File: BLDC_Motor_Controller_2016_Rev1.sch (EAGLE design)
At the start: 99 parts, among them J1 SERVOMOLEX_SL_THRU_HOLE, J2 SL03THROUGH_HOLE, J3 APP_2POS_CONFIG5V_HORIZ, Q1 MOSFET-NCHANNELFQP30N06L, Q2 MOSFET-NCHANNELFQP30N06L, Q3 MOSFET-NCHANNELFQP30N06L, Q4 MOSFET-NCHANNELFQP30N06L, Q5 MOSFET-NCHANNELFQP30N06L, Q6 MOSFET-NCHANNELFQP30N06L, Q7 MOSFET-PCHANNEL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

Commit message: Added RS-485 IC to replace UART
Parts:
- removed J2: SL03THROUGH_HOLE, MRDT-Connectors:SL03THROUGH_HOLE
- added R30, R31: 3.3, SparkFun-Passives:RESISTOR0805-RES
- added U$3: MAX3077, MRDT-2015-General:MAX3077
- added U$4: 5PIN, Molex-SL:5PIN
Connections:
- new net N$34: R30.2, U$3.Y, U$4.4
- new net N$36: R30.1, U$3.Z, U$4.3
- new net N$37: R31.2, U$3.B, U$4.2
- new net N$38: R31.1, U$3.A, U$4.1
- net GND: now also U$3.GND, U$4.5; no longer J2.1
- net RX: now also U$3.RO; no longer J2.2
- net TX: now also U$3.DI; no longer J2.3
- net VCC: now also U$3.VCC
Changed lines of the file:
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@@
 <?xml version="1.0" encoding="utf-8"?>
 <!DOCTYPE eagle SYSTEM "eagle.dtd">
-<eagle version="7.3.0">
+<eagle version="7.1.0">
 <drawing>
 <settings>
@@
 <part name="C35" library="SparkFun-Passives" deviceset="CAP_POL" device="PTH4" value="220u"/>
 <part name="GND35" library="SparkFun-Aesthetics" deviceset="GND" device=""/>
-<part name="J2" library="MRDT-Connectors" deviceset="SL03" device="THROUGH_HOLE"/>
-<part name="GND34" library="SparkFun-Aesthetics" deviceset="GND" device=""/>
 <part name="J1" library="MRDT-Connectors" deviceset="SERVO" device="MOLEX_SL_THRU_HOLE"/>
 <part name="J3" library="MRDT-Connectors" deviceset="APP_2POS_CONFIG" device="5V_HORIZ"/>
 <part name="C38" library="SparkFun-Passives" deviceset="CAP_POL" device="PTH4" value="220u"/>
+<part name="U$3" library="MRDT-2015-General" deviceset="MAX3077" device=""/>
+<part name="R30" library="SparkFun-Passives" deviceset="RESISTOR" device="0805-RES" value="3.3"/>
+<part name="R31" library="SparkFun-Passives" deviceset="RESISTOR" device="0805-RES" value="3.3"/>
+<part name="U$4" library="Molex-SL" deviceset="5PIN" device=""/>
+<part name="GND36" library="SparkFun-Aesthetics" deviceset="GND" device=""/>
+<part name="GND37" library="SparkFun-Aesthetics" deviceset="GND" device=""/>
 </parts>
 <sheets>
@@
 <instance part="C35" gate="G$1" x="-63.5" y="-121.92"/>
 <instance part="GND35" gate="1" x="274.32" y="-195.58"/>
-<instance part="J2" gate="G$1" x="289.56" y="-167.64"/>
-<instance part="GND34" gate="1" x="276.86" y="-175.26"/>
 <instance part="J1" gate="G$1" x="284.48" y="-193.04"/>
 <instance part="J3" gate="GND" x="256.54" y="-53.34"/>
 <instance part="J3" gate="VCC" x="256.54" y="-45.72"/>
 <instance part="C38" gate="G$1" x="-73.66" y="-121.92"/>
+<instance part="U$3" gate="G$1" x="-121.92" y="-96.52"/>
+<instance part="R30" gate="G$1" x="-106.68" y="-91.44"/>
+<instance part="R31" gate="G$1" x="-106.68" y="-81.28"/>
+<instance part="U$4" gate="G$1" x="-86.36" y="-91.44"/>
+<instance part="GND36" gate="1" x="-96.52" y="-104.14"/>
+<instance part="GND37" gate="1" x="-147.32" y="-101.6"/>
 </instances>
 <busses>
@@
 </segment>
 <segment>
-<pinref part="J2" gate="G$1" pin="1"/>
-<wire x1="281.94" y1="-170.18" x2="276.86" y2="-170.18" width="0.1524" layer="91"/>
-<wire x1="276.86" y1="-170.18" x2="276.86" y2="-172.72" width="0.1524" layer="91"/>
-<pinref part="GND34" gate="1" pin="GND"/>
+<pinref part="U$4" gate="G$1" pin="5"/>
+<pinref part="GND36" gate="1" pin="GND"/>
+<wire x1="-93.98" y1="-99.06" x2="-96.52" y2="-99.06" width="0.1524" layer="91"/>
+<wire x1="-96.52" y1="-99.06" x2="-96.52" y2="-101.6" width="0.1524" layer="91"/>
+</segment>
+<segment>
+<pinref part="U$3" gate="G$1" pin="GND"/>
+<pinref part="GND37" gate="1" pin="GND"/>
+<wire x1="-144.78" y1="-93.98" x2="-147.32" y2="-93.98" width="0.1524" layer="91"/>
+<wire x1="-147.32" y1="-93.98" x2="-147.32" y2="-99.06" width="0.1524" layer="91"/>
 </segment>
 </net>
@@
 <pinref part="U$13" gate="G$1" pin="VCC"/>
 <pinref part="SUPPLY9" gate="G$1" pin="VCC"/>
+</segment>
+<segment>
+<pinref part="U$3" gate="G$1" pin="VCC"/>
+<wire x1="-144.78" y1="-78.74" x2="-147.32" y2="-78.74" width="0.1524" layer="91"/>
+<wire x1="-147.32" y1="-78.74" x2="-147.32" y2="-73.66" width="0.1524" layer="91"/>
+<label x="-147.32" y="-73.66" size="1.778" layer="95" rot="R90" xref="yes"/>
 </segment>
 </net>
@@
 </segment>
 <segment>
-<pinref part="J2" gate="G$1" pin="3"/>
-<wire x1="281.94" y1="-165.1" x2="276.86" y2="-165.1" width="0.1524" layer="91"/>
-<label x="276.86" y="-165.1" size="1.778" layer="95" rot="R180" xref="yes"/>
+<pinref part="U$3" gate="G$1" pin="DI"/>
+<wire x1="-144.78" y1="-88.9" x2="-147.32" y2="-88.9" width="0.1524" layer="91"/>
+<label x="-147.32" y="-88.9" size="1.778" layer="95" rot="R180" xref="yes"/>
 </segment>
 </net>
@@
 </segment>
 <segment>
-<pinref part="J2" gate="G$1" pin="2"/>
-<wire x1="281.94" y1="-167.64" x2="276.86" y2="-167.64" width="0.1524" layer="91"/>
-<label x="276.86" y="-167.64" size="1.778" layer="95" rot="R180" xref="yes"/>
+<pinref part="U$3" gate="G$1" pin="RO"/>
+<wire x1="-144.78" y1="-83.82" x2="-147.32" y2="-83.82" width="0.1524" layer="91"/>
+<label x="-147.32" y="-83.82" size="1.778" layer="95" rot="R180" xref="yes"/>
 </segment>
 </net>
@@
 </segment>
 </net>
+<net name="N$34" class="0">
+<segment>
+<pinref part="U$3" gate="G$1" pin="Y"/>
+<pinref part="U$4" gate="G$1" pin="4"/>
+<wire x1="-116.84" y1="-93.98" x2="-99.06" y2="-93.98" width="0.1524" layer="91"/>
+<pinref part="R30" gate="G$1" pin="2"/>
+<wire x1="-99.06" y1="-93.98" x2="-93.98" y2="-93.98" width="0.1524" layer="91"/>
+<wire x1="-101.6" y1="-91.44" x2="-99.06" y2="-91.44" width="0.1524" layer="91"/>
+<wire x1="-99.06" y1="-91.44" x2="-99.06" y2="-93.98" width="0.1524" layer="91"/>
+<junction x="-99.06" y="-93.98"/>
+</segment>
+</net>
+<net name="N$36" class="0">
+<segment>
+<pinref part="U$3" gate="G$1" pin="Z"/>
+<pinref part="U$4" gate="G$1" pin="3"/>
+<wire x1="-116.84" y1="-88.9" x2="-114.3" y2="-88.9" width="0.1524" layer="91"/>
+<pinref part="R30" gate="G$1" pin="1"/>
+<wire x1="-114.3" y1="-88.9" x2="-93.98" y2="-88.9" width="0.1524" layer="91"/>
+<wire x1="-111.76" y1="-91.44" x2="-114.3" y2="-91.44" width="0.1524" layer="91"/>
+<wire x1="-114.3" y1="-91.44" x2="-114.3" y2="-88.9" width="0.1524" layer="91"/>
+<junction x="-114.3" y="-88.9"/>
+</segment>
+</net>
+<net name="N$37" class="0">
+<segment>
+<pinref part="U$3" gate="G$1" pin="B"/>
+<pinref part="U$4" gate="G$1" pin="2"/>
+<wire x1="-116.84" y1="-83.82" x2="-99.06" y2="-83.82" width="0.1524" layer="91"/>
+<pinref part="R31" gate="G$1" pin="2"/>
+<wire x1="-99.06" y1="-83.82" x2="-93.98" y2="-83.82" width="0.1524" layer="91"/>
+<wire x1="-101.6" y1="-81.28" x2="-99.06" y2="-81.28" width="0.1524" layer="91"/>
+<wire x1="-99.06" y1="-81.28" x2="-99.06" y2="-83.82" width="0.1524" layer="91"/>
+<junction x="-99.06" y="-83.82"/>
+</segment>
+</net>
+<net name="N$38" class="0">
+<segment>
+<pinref part="U$3" gate="G$1" pin="A"/>
+<pinref part="U$4" gate="G$1" pin="1"/>
+<wire x1="-116.84" y1="-78.74" x2="-114.3" y2="-78.74" width="0.1524" layer="91"/>
+<pinref part="R31" gate="G$1" pin="1"/>
+<wire x1="-114.3" y1="-78.74" x2="-93.98" y2="-78.74" width="0.1524" layer="91"/>
+<wire x1="-111.76" y1="-81.28" x2="-114.3" y2="-81.28" width="0.1524" layer="91"/>
+<wire x1="-114.3" y1="-81.28" x2="-114.3" y2="-78.74" width="0.1524" layer="91"/>
+<junction x="-114.3" y="-78.74"/>
+</segment>
+</net>

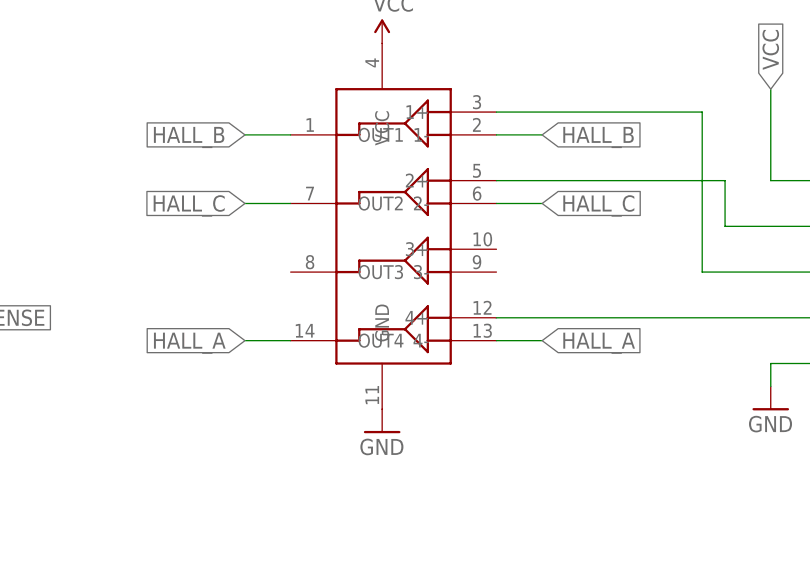
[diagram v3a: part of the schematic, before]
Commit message: Improved routing
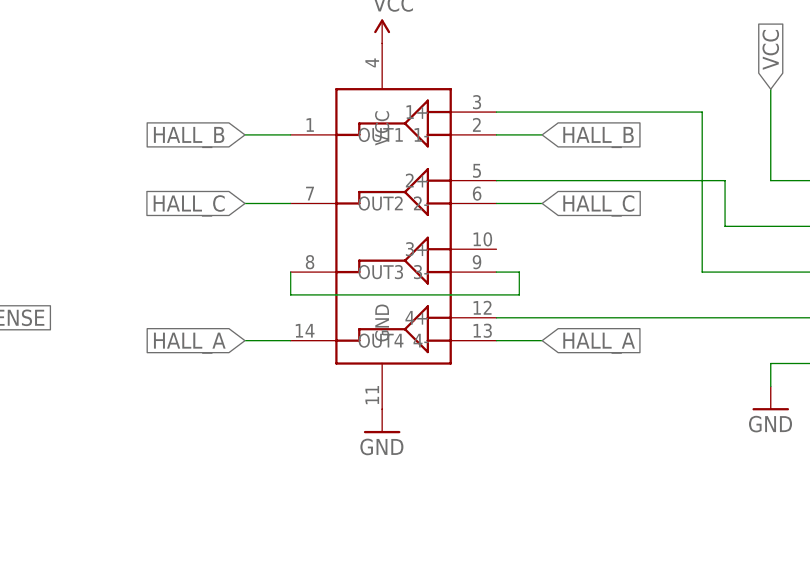
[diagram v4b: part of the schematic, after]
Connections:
- new net N$40: U$13.3-, U$13.OUT3
- new net SP1: C21.2, R13.1, U$1.SP1
- new net SP2: C24.2, R18.1, U$1.SP2
- net GND: no longer C21.2, C24.2, R13.1, R18.1, U$1.SP1, U$1.SP2
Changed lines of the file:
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@@
 <?xml version="1.0" encoding="utf-8"?>
 <!DOCTYPE eagle SYSTEM "eagle.dtd">
-<eagle version="7.1.0">
+<eagle version="7.3.0">
 <drawing>
 <settings>
@@
 </segment>
 <segment>
-<wire x1="142.24" y1="-73.66" x2="142.24" y2="-78.74" width="0.1524" layer="91"/>
-<wire x1="142.24" y1="-73.66" x2="129.54" y2="-73.66" width="0.1524" layer="91"/>
-<pinref part="GND17" gate="1" pin="GND"/>
-<pinref part="C24" gate="G$1" pin="2"/>
-<wire x1="129.54" y1="-71.12" x2="129.54" y2="-73.66" width="0.1524" layer="91"/>
-<wire x1="129.54" y1="-73.66" x2="63.5" y2="-73.66" width="0.1524" layer="91"/>
-<wire x1="63.5" y1="-73.66" x2="63.5" y2="-55.88" width="0.1524" layer="91"/>
-<junction x="129.54" y="-73.66"/>
-<pinref part="U$1" gate="G$1" pin="SP2"/>
-<wire x1="63.5" y1="-55.88" x2="17.78" y2="-55.88" width="0.1524" layer="91"/>
-<pinref part="R18" gate="G$1" pin="1"/>
-<junction x="142.24" y="-73.66"/>
-</segment>
-<segment>
-<wire x1="142.24" y1="7.62" x2="142.24" y2="2.54" width="0.1524" layer="91"/>
-<wire x1="142.24" y1="7.62" x2="129.54" y2="7.62" width="0.1524" layer="91"/>
-<pinref part="GND14" gate="1" pin="GND"/>
-<pinref part="C21" gate="G$1" pin="2"/>
-<wire x1="129.54" y1="10.16" x2="129.54" y2="7.62" width="0.1524" layer="91"/>
-<wire x1="129.54" y1="7.62" x2="81.28" y2="7.62" width="0.1524" layer="91"/>
-<junction x="129.54" y="7.62"/>
-<wire x1="81.28" y1="7.62" x2="81.28" y2="-45.72" width="0.1524" layer="91"/>
-<pinref part="U$1" gate="G$1" pin="SP1"/>
-<wire x1="81.28" y1="-45.72" x2="17.78" y2="-45.72" width="0.1524" layer="91"/>
-<pinref part="R13" gate="G$1" pin="1"/>
-<junction x="142.24" y="7.62"/>
-</segment>
-<segment>
 <pinref part="GND20" gate="1" pin="GND"/>
 <pinref part="Q6" gate="G$1" pin="S"/>
@@
 </segment>
 </net>
+<net name="N$40" class="0">
+<segment>
+<pinref part="U$13" gate="G$1" pin="3-"/>
+<wire x1="246.38" y1="-134.62" x2="248.92" y2="-134.62" width="0.1524" layer="91"/>
+<wire x1="248.92" y1="-134.62" x2="248.92" y2="-137.16" width="0.1524" layer="91"/>
+<pinref part="U$13" gate="G$1" pin="OUT3"/>
+<wire x1="248.92" y1="-137.16" x2="223.52" y2="-137.16" width="0.1524" layer="91"/>
+<wire x1="223.52" y1="-137.16" x2="223.52" y2="-134.62" width="0.1524" layer="91"/>
+</segment>
+</net>
+<net name="SP1" class="0">
+<segment>
+<wire x1="142.24" y1="7.62" x2="142.24" y2="2.54" width="0.1524" layer="91"/>
+<wire x1="142.24" y1="7.62" x2="129.54" y2="7.62" width="0.1524" layer="91"/>
+<pinref part="GND14" gate="1" pin="GND"/>
+<pinref part="C21" gate="G$1" pin="2"/>
+<wire x1="129.54" y1="10.16" x2="129.54" y2="7.62" width="0.1524" layer="91"/>
+<wire x1="129.54" y1="7.62" x2="81.28" y2="7.62" width="0.1524" layer="91"/>
+<junction x="129.54" y="7.62"/>
+<wire x1="81.28" y1="7.62" x2="81.28" y2="-45.72" width="0.1524" layer="91"/>
+<pinref part="U$1" gate="G$1" pin="SP1"/>
+<wire x1="81.28" y1="-45.72" x2="17.78" y2="-45.72" width="0.1524" layer="91"/>
+<pinref part="R13" gate="G$1" pin="1"/>
+<junction x="142.24" y="7.62"/>
+</segment>
+</net>
+<net name="SP2" class="0">
+<segment>
+<wire x1="142.24" y1="-73.66" x2="142.24" y2="-78.74" width="0.1524" layer="91"/>
+<wire x1="142.24" y1="-73.66" x2="129.54" y2="-73.66" width="0.1524" layer="91"/>
+<pinref part="GND17" gate="1" pin="GND"/>
+<pinref part="C24" gate="G$1" pin="2"/>
+<wire x1="129.54" y1="-71.12" x2="129.54" y2="-73.66" width="0.1524" layer="91"/>
+<wire x1="129.54" y1="-73.66" x2="63.5" y2="-73.66" width="0.1524" layer="91"/>
+<wire x1="63.5" y1="-73.66" x2="63.5" y2="-55.88" width="0.1524" layer="91"/>
+<junction x="129.54" y="-73.66"/>
+<pinref part="U$1" gate="G$1" pin="SP2"/>
+<wire x1="63.5" y1="-55.88" x2="17.78" y2="-55.88" width="0.1524" layer="91"/>
+<pinref part="R18" gate="G$1" pin="1"/>
+<junction x="142.24" y="-73.66"/>
+</segment>
+</net>

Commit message: Half duplex RS485, single 5-pin SL connector on left side
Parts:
- removed J1: SERVOMOLEX_SL_THRU_HOLE, MRDT-Connectors:SERVOMOLEX_SL_THRU_HOLE
- removed R31: 3.3, SparkFun-Passives:RESISTOR0805-RES
- added C39: 220u, SparkFun-Passives:CAP_POLPTH4
- R30: value 3.3 -> 120
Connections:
- removed net N$37: R31.2, U$3.B, U$4.2
- removed net N$38: R31.1, U$3.A, U$4.1
- net GND: now also C39.-, U$4.3; no longer J1.GND, U$4.5
- net N$34: now also U$3.B, U$3.Z, U$4.2; no longer U$3.Y, U$4.4
- net N$36: now also U$3.A, U$3.Y, U$4.1; no longer U$3.Z, U$4.3
- net PVDD: now also C39.+
- net SPEED_IN: now also U$4.4; no longer J1.SIG
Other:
- moved on the sheet: R30
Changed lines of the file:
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@@
 <part name="C34" library="SparkFun-Passives" deviceset="CAP_POL" device="PTH4" value="220u"/>
 <part name="C35" library="SparkFun-Passives" deviceset="CAP_POL" device="PTH4" value="220u"/>
-<part name="GND35" library="SparkFun-Aesthetics" deviceset="GND" device=""/>
-<part name="J1" library="MRDT-Connectors" deviceset="SERVO" device="MOLEX_SL_THRU_HOLE"/>
 <part name="J3" library="MRDT-Connectors" deviceset="APP_2POS_CONFIG" device="5V_HORIZ"/>
 <part name="C38" library="SparkFun-Passives" deviceset="CAP_POL" device="PTH4" value="220u"/>
 <part name="U$3" library="MRDT-2015-General" deviceset="MAX3077" device=""/>
-<part name="R30" library="SparkFun-Passives" deviceset="RESISTOR" device="0805-RES" value="3.3"/>
-<part name="R31" library="SparkFun-Passives" deviceset="RESISTOR" device="0805-RES" value="3.3"/>
+<part name="R30" library="SparkFun-Passives" deviceset="RESISTOR" device="0805-RES" value="120"/>
 <part name="U$4" library="Molex-SL" deviceset="5PIN" device=""/>
 <part name="GND36" library="SparkFun-Aesthetics" deviceset="GND" device=""/>
 <part name="GND37" library="SparkFun-Aesthetics" deviceset="GND" device=""/>
+<part name="C39" library="SparkFun-Passives" deviceset="CAP_POL" device="PTH4" value="220u"/>
 </parts>
 <sheets>
@@
 <instance part="C34" gate="G$1" x="-53.34" y="-121.92"/>
 <instance part="C35" gate="G$1" x="-63.5" y="-121.92"/>
-<instance part="GND35" gate="1" x="274.32" y="-195.58"/>
-<instance part="J1" gate="G$1" x="284.48" y="-193.04"/>
 <instance part="J3" gate="GND" x="256.54" y="-53.34"/>
 <instance part="J3" gate="VCC" x="256.54" y="-45.72"/>
 <instance part="C38" gate="G$1" x="-73.66" y="-121.92"/>
 <instance part="U$3" gate="G$1" x="-121.92" y="-96.52"/>
-<instance part="R30" gate="G$1" x="-106.68" y="-91.44"/>
-<instance part="R31" gate="G$1" x="-106.68" y="-81.28"/>
-<instance part="U$4" gate="G$1" x="-86.36" y="-91.44"/>
-<instance part="GND36" gate="1" x="-96.52" y="-104.14"/>
+<instance part="R30" gate="G$1" x="-101.6" y="-81.28"/>
+<instance part="U$4" gate="G$1" x="-81.28" y="-91.44"/>
+<instance part="GND36" gate="1" x="-93.98" y="-88.9" rot="R270"/>
 <instance part="GND37" gate="1" x="-147.32" y="-101.6"/>
+<instance part="C39" gate="G$1" x="-83.82" y="-121.92"/>
 </instances>
 <busses>
@@
 <wire x1="-73.66" y1="-137.16" x2="-63.5" y2="-137.16" width="0.1524" layer="91"/>
 <junction x="-63.5" y="-137.16"/>
+<pinref part="C39" gate="G$1" pin="-"/>
+<wire x1="-73.66" y1="-137.16" x2="-83.82" y2="-137.16" width="0.1524" layer="91"/>
+<wire x1="-83.82" y1="-137.16" x2="-83.82" y2="-127" width="0.1524" layer="91"/>
+<junction x="-73.66" y="-137.16"/>
 </segment>
 <segment>
@@
 </segment>
 <segment>
-<wire x1="279.4" y1="-190.5" x2="274.32" y2="-190.5" width="0.1524" layer="91"/>
-<pinref part="GND35" gate="1" pin="GND"/>
-<wire x1="274.32" y1="-190.5" x2="274.32" y2="-193.04" width="0.1524" layer="91"/>
-<pinref part="J1" gate="G$1" pin="GND"/>
-</segment>
-<segment>
-<pinref part="U$4" gate="G$1" pin="5"/>
-<pinref part="GND36" gate="1" pin="GND"/>
-<wire x1="-93.98" y1="-99.06" x2="-96.52" y2="-99.06" width="0.1524" layer="91"/>
-<wire x1="-96.52" y1="-99.06" x2="-96.52" y2="-101.6" width="0.1524" layer="91"/>
-</segment>
-<segment>
 <pinref part="U$3" gate="G$1" pin="GND"/>
 <pinref part="GND37" gate="1" pin="GND"/>
 <wire x1="-144.78" y1="-93.98" x2="-147.32" y2="-93.98" width="0.1524" layer="91"/>
 <wire x1="-147.32" y1="-93.98" x2="-147.32" y2="-99.06" width="0.1524" layer="91"/>
+</segment>
+<segment>
+<pinref part="U$4" gate="G$1" pin="3"/>
+<pinref part="GND36" gate="1" pin="GND"/>
+<wire x1="-88.9" y1="-88.9" x2="-91.44" y2="-88.9" width="0.1524" layer="91"/>
 </segment>
 </net>
@@
 <wire x1="-73.66" y1="-114.3" x2="-73.66" y2="-119.38" width="0.1524" layer="91"/>
 <junction x="-63.5" y="-114.3"/>
+<pinref part="C39" gate="G$1" pin="+"/>
+<wire x1="-73.66" y1="-114.3" x2="-83.82" y2="-114.3" width="0.1524" layer="91"/>
+<wire x1="-83.82" y1="-114.3" x2="-83.82" y2="-119.38" width="0.1524" layer="91"/>
+<junction x="-73.66" y="-114.3"/>
 </segment>
 <segment>
@@
 </segment>
 <segment>
-<wire x1="279.4" y1="-187.96" x2="274.32" y2="-187.96" width="0.1524" layer="91"/>
-<label x="274.32" y="-187.96" size="1.778" layer="95" rot="R180" xref="yes"/>
-<pinref part="J1" gate="G$1" pin="SIG"/>
-</segment>
-</net>
-<net name="N$34" class="0">
-<segment>
-<pinref part="U$3" gate="G$1" pin="Y"/>
 <pinref part="U$4" gate="G$1" pin="4"/>
-<wire x1="-116.84" y1="-93.98" x2="-99.06" y2="-93.98" width="0.1524" layer="91"/>
-<pinref part="R30" gate="G$1" pin="2"/>
-<wire x1="-99.06" y1="-93.98" x2="-93.98" y2="-93.98" width="0.1524" layer="91"/>
-<wire x1="-101.6" y1="-91.44" x2="-99.06" y2="-91.44" width="0.1524" layer="91"/>
-<wire x1="-99.06" y1="-91.44" x2="-99.06" y2="-93.98" width="0.1524" layer="91"/>
-<junction x="-99.06" y="-93.98"/>
-</segment>
-</net>
-<net name="N$36" class="0">
-<segment>
-<pinref part="U$3" gate="G$1" pin="Z"/>
-<pinref part="U$4" gate="G$1" pin="3"/>
-<wire x1="-116.84" y1="-88.9" x2="-114.3" y2="-88.9" width="0.1524" layer="91"/>
-<pinref part="R30" gate="G$1" pin="1"/>
-<wire x1="-114.3" y1="-88.9" x2="-93.98" y2="-88.9" width="0.1524" layer="91"/>
-<wire x1="-111.76" y1="-91.44" x2="-114.3" y2="-91.44" width="0.1524" layer="91"/>
-<wire x1="-114.3" y1="-91.44" x2="-114.3" y2="-88.9" width="0.1524" layer="91"/>
-<junction x="-114.3" y="-88.9"/>
-</segment>
-</net>
-<net name="N$37" class="0">
-<segment>
-<pinref part="U$3" gate="G$1" pin="B"/>
-<pinref part="U$4" gate="G$1" pin="2"/>
-<wire x1="-116.84" y1="-83.82" x2="-99.06" y2="-83.82" width="0.1524" layer="91"/>
-<pinref part="R31" gate="G$1" pin="2"/>
-<wire x1="-99.06" y1="-83.82" x2="-93.98" y2="-83.82" width="0.1524" layer="91"/>
-<wire x1="-101.6" y1="-81.28" x2="-99.06" y2="-81.28" width="0.1524" layer="91"/>
-<wire x1="-99.06" y1="-81.28" x2="-99.06" y2="-83.82" width="0.1524" layer="91"/>
-<junction x="-99.06" y="-83.82"/>
-</segment>
-</net>
-<net name="N$38" class="0">
-<segment>
-<pinref part="U$3" gate="G$1" pin="A"/>
-<pinref part="U$4" gate="G$1" pin="1"/>
-<wire x1="-116.84" y1="-78.74" x2="-114.3" y2="-78.74" width="0.1524" layer="91"/>
-<pinref part="R31" gate="G$1" pin="1"/>
-<wire x1="-114.3" y1="-78.74" x2="-93.98" y2="-78.74" width="0.1524" layer="91"/>
-<wire x1="-111.76" y1="-81.28" x2="-114.3" y2="-81.28" width="0.1524" layer="91"/>
-<wire x1="-114.3" y1="-81.28" x2="-114.3" y2="-78.74" width="0.1524" layer="91"/>
-<junction x="-114.3" y="-78.74"/>
+<wire x1="-88.9" y1="-93.98" x2="-91.44" y2="-93.98" width="0.1524" layer="91"/>
+<label x="-91.44" y="-93.98" size="1.778" layer="95" rot="R180" xref="yes"/>
 </segment>
 </net>
@@
 </segment>
 </net>
+<net name="N$34" class="0">
+<segment>
+<pinref part="U$3" gate="G$1" pin="B"/>
+<pinref part="U$3" gate="G$1" pin="Z"/>
+<wire x1="-116.84" y1="-83.82" x2="-116.84" y2="-88.9" width="0.1524" layer="91"/>
+<pinref part="U$4" gate="G$1" pin="2"/>
+<wire x1="-116.84" y1="-83.82" x2="-96.52" y2="-83.82" width="0.1524" layer="91"/>
+<junction x="-116.84" y="-83.82"/>
+<pinref part="R30" gate="G$1" pin="2"/>
+<wire x1="-96.52" y1="-83.82" x2="-88.9" y2="-83.82" width="0.1524" layer="91"/>
+<wire x1="-96.52" y1="-81.28" x2="-96.52" y2="-83.82" width="0.1524" layer="91"/>
+<junction x="-96.52" y="-83.82"/>
+</segment>
+</net>
+<net name="N$36" class="0">
+<segment>
+<pinref part="U$3" gate="G$1" pin="A"/>
+<wire x1="-116.84" y1="-78.74" x2="-114.3" y2="-78.74" width="0.1524" layer="91"/>
+<wire x1="-114.3" y1="-78.74" x2="-114.3" y2="-93.98" width="0.1524" layer="91"/>
+<pinref part="U$3" gate="G$1" pin="Y"/>
+<wire x1="-114.3" y1="-93.98" x2="-116.84" y2="-93.98" width="0.1524" layer="91"/>
+<pinref part="U$4" gate="G$1" pin="1"/>
+<wire x1="-114.3" y1="-78.74" x2="-106.68" y2="-78.74" width="0.1524" layer="91"/>
+<junction x="-114.3" y="-78.74"/>
+<pinref part="R30" gate="G$1" pin="1"/>
+<wire x1="-106.68" y1="-78.74" x2="-88.9" y2="-78.74" width="0.1524" layer="91"/>
+<wire x1="-106.68" y1="-81.28" x2="-106.68" y2="-78.74" width="0.1524" layer="91"/>
+<junction x="-106.68" y="-78.74"/>
+</segment>
+</net>
